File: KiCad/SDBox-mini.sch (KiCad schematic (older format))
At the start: 31 parts, among them J1 DB25_Male, J2 Conn_01x06, J3 Micro_SD_Card, J4 USB_B_Micro, Q1 BC857CW, U1 ATmega328P-AU, U2 LM1117-3.3, U3 74LVC3G17, U4 74HCT2G17, Y1 Crystal_GND24_Small

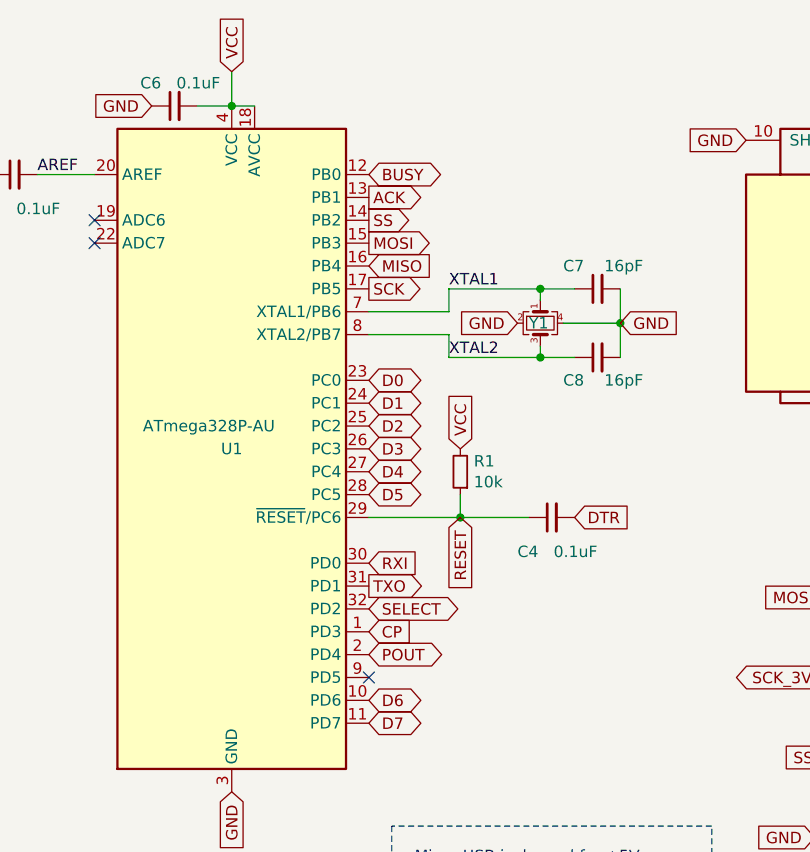
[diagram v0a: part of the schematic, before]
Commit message: Changed pin assignment BUSY from PB0 to PD4, POUT from PD4 to PD5 and rerouted due to change in FW.
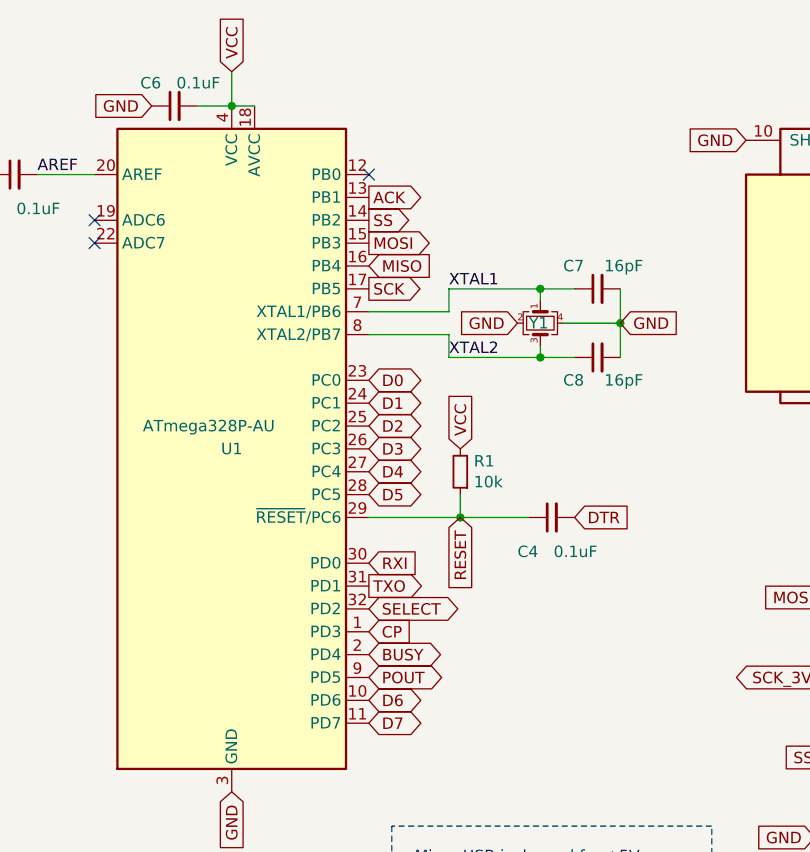
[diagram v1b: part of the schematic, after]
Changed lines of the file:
@@
 Wire Wire Line
 	5650 2250 5650 2400
+Text GLabel 4550 3800 2    50   BiDi ~ 0
+POUT
 Text GLabel 4550 3700 2    50   BiDi ~ 0
-POUT
-Text GLabel 4550 1600 2    50   BiDi ~ 0
 BUSY
 Text GLabel 4550 3300 2    50   Input ~ 0
@@
 	4950 3100 5250 3100
 Connection ~ 4950 3100
-NoConn ~ 4550 3800
+NoConn ~ 4550 1600
 NoConn ~ 7900 2350
 Text GLabel 10200 3400 2    50   Output ~ 0

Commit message: removed FTDI-header, added ICSP-header, removed hw-debounce circuit and rerouted
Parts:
- removed C11, C4: 0.1uF, Capacitor_SMD:C_0603_1608Metric_Pad1.05x0.95mm_HandSolder, symbol Device:C_Small
- removed J2: Conn_01x06, Connector_PinHeader_2.54mm:PinHeader_1x06_P2.54mm_Vertical, symbol Connector_Generic:Conn_01x06
- removed R3, R4: 10k, Resistor_SMD:R_0603_1608Metric_Pad1.05x0.95mm_HandSolder, symbol Device:R_Small
- added J2: Conn_02x03_Odd_Even, Connector_PinHeader_2.54mm:PinHeader_2x03_P2.54mm_Vertical, symbol Connector_Generic:Conn_02x03_Odd_Even
- renumbered C8 to C10, C12 to C4, C9 to C5, C10 to C6, C5 to C7, C6 to C8, C7 to C9, R5 to R3, R6 to R4, R7 to R5
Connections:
- net labels removed: CD, DTR, RXI, TXO
- wire segments 58 -> 52
- no-connect marks 14 -> 17
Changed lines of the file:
@@
 $EndDescr
 $Comp
-L Device:C_Small C5
+L Device:C_Small C7
 U 1 1 606A3110
 P 3000 1600
-F 0 "C5" V 2850 1750 50  0000 R CNN
+F 0 "C7" V 2850 1750 50  0000 R CNN
 F 1 "0.1uF" V 2850 1400 50  0000 L CNN
 F 2 "Capacitor_SMD:C_0603_1608Metric_Pad1.05x0.95mm_HandSolder" H 3000 1600 50  0001 C CNN
@@
 GND
 $Comp
-L Device:C_Small C7
+L Device:C_Small C9
 U 1 1 60FA06FB
 P 5550 2100
-F 0 "C7" V 5650 2250 50  0000 R CNN
+F 0 "C9" V 5650 2250 50  0000 R CNN
 F 1 "16pF" V 5650 1900 50  0000 L CNN
 F 2 "Capacitor_SMD:C_0603_1608Metric_Pad1.05x0.95mm_HandSolder" H 5550 2100 50  0001 C CNN
@@
 	4900 2100 5300 2100
 $Comp
-L Device:C_Small C8
+L Device:C_Small C10
 U 1 1 60FA5116
 P 5550 2400
-F 0 "C8" V 5450 2550 50  0000 R CNN
+F 0 "C10" V 5450 2550 50  0000 R CNN
 F 1 "16pF" V 5450 2200 50  0000 L CNN
 F 2 "Capacitor_SMD:C_0603_1608Metric_Pad1.05x0.95mm_HandSolder" H 5550 2400 50  0001 C CNN
@@
 Connection ~ 5650 2250
 $Comp
-L Device:C_Small C6
+L Device:C_Small C8
 U 1 1 60FA7C64
 P 3700 1300
-F 0 "C6" V 3800 1450 50  0000 R CNN
+F 0 "C8" V 3800 1450 50  0000 R CNN
 F 1 "0.1uF" V 3800 1100 50  0000 L CNN
 F 2 "Capacitor_SMD:C_0603_1608Metric_Pad1.05x0.95mm_HandSolder" H 3700 1300 50  0001 C CNN
@@
 Text GLabel 4550 3700 2    50   BiDi ~ 0
 BUSY
-Text GLabel 4550 3300 2    50   Input ~ 0
-RXI
-Text GLabel 4550 3400 2    50   Output ~ 0
-TXO
 NoConn ~ 2000 3950
 Text GLabel 4550 2000 2    50   Input ~ 0
@@
 Wire Wire Line
 	4550 2300 4900 2300
-Text GLabel 5450 3100 2    50   Input ~ 0
-DTR
-$Comp
-L Device:C_Small C4
-U 1 1 60F8E9CC
-P 5350 3100
-F 0 "C4" V 5200 3250 50  0000 R CNN
-F 1 "0.1uF" V 5200 2900 50  0000 L CNN
-F 2 "Capacitor_SMD:C_0603_1608Metric_Pad1.05x0.95mm_HandSolder" H 5350 3100 50  0001 C CNN
-F 3 "~" H 5350 3100 50  0001 C CNN
-	1    5350 3100
-	0    -1   -1   0
-$EndComp
-Text GLabel 4950 3100 3    50   Input ~ 0
+Text GLabel 4950 3100 2    50   Input ~ 0
 RESET
-Wire Wire Line
-	4950 3100 5250 3100
-Connection ~ 4950 3100
 NoConn ~ 4550 1600
 NoConn ~ 7900 2350
@@
 Text GLabel 10500 1750 2    50   Output ~ 0
 3V3
-$Comp
-L Connector_Generic:Conn_01x06 J2
-U 1 1 6104A5C2
-P 2200 5000
-F 0 "J2" H 2118 4475 50  0000 C CNN
-F 1 "Conn_01x06" H 2118 4566 50  0000 C CNN
-F 2 "Connector_PinHeader_2.54mm:PinHeader_1x06_P2.54mm_Vertical" H 2200 5000 50  0001 C CNN
-F 3 "~" H 2200 5000 50  0001 C CNN
-	1    2200 5000
-	-1   0    0    1
-$EndComp
-Text GLabel 2400 5200 2    50   Input ~ 0
-DTR
-Text GLabel 2400 5100 2    50   Input ~ 0
-TXO
-Text GLabel 2400 5000 2    50   Output ~ 0
-RXI
-Text GLabel 2400 4900 2    50   Input ~ 0
-VCC
-Text GLabel 2400 4800 2    50   Input ~ 0
-GND
-Text GLabel 2400 4700 2    50   Input ~ 0
-GND
-$Comp
-L Device:C_Small C9
+Text GLabel 3400 4950 2    50   Input ~ 0
+VCC
+Text GLabel 3400 5150 2    50   Input ~ 0
+GND
+$Comp
+L Device:C_Small C5
 U 1 1 61017825
 P 7550 3350
-F 0 "C9" H 7400 3250 50  0000 R CNN
+F 0 "C5" H 7400 3250 50  0000 R CNN
 F 1 "0.1uF" H 7200 3350 50  0000 L CNN
 F 2 "Capacitor_SMD:C_0603_1608Metric_Pad1.05x0.95mm_HandSolder" H 7550 3350 50  0001 C CNN
@@
 $EndComp
 $Comp
-L Device:C_Small C10
+L Device:C_Small C6
 U 1 1 61087309
 P 10700 3500
-F 0 "C10" H 10550 3400 50  0000 R CNN
+F 0 "C6" H 10550 3400 50  0000 R CNN
 F 1 "0.1uF" H 10350 3500 50  0000 L CNN
 F 2 "Capacitor_SMD:C_0603_1608Metric_Pad1.05x0.95mm_HandSolder" H 10700 3500 50  0001 C CNN
@@
 	9050 3400 9300 3400
 Connection ~ 9050 3400
-Text GLabel 9050 3600 0    50   Input ~ 0
-GND
-$Comp
-L Device:R_Small R4
-U 1 1 61098AA5
-P 8350 3700
-F 0 "R4" H 8291 3654 50  0000 R CNN
-F 1 "10k" H 8291 3745 50  0000 R CNN
-F 2 "Resistor_SMD:R_0603_1608Metric_Pad1.05x0.95mm_HandSolder" H 8350 3700 50  0001 C CNN
-F 3 "~" H 8350 3700 50  0001 C CNN
-	1    8350 3700
-	-1   0    0    1
-$EndComp
+Text GLabel 9300 3600 0    50   Input ~ 0
+GND
 Wire Wire Line
 	9250 1950 9250 2050
@@
 GND
 Text GLabel 7900 1450 2    50   Output ~ 0
-CD
-Text GLabel 8350 3600 1    50   Input ~ 0
-VCC
-$Comp
-L Device:R_Small R3
-U 1 1 610BDC67
-P 8800 3800
-F 0 "R3" V 8900 3850 50  0000 R CNN
-F 1 "10k" V 8700 3850 50  0000 R CNN
-F 2 "Resistor_SMD:R_0603_1608Metric_Pad1.05x0.95mm_HandSolder" H 8800 3800 50  0001 C CNN
-F 3 "~" H 8800 3800 50  0001 C CNN
-	1    8800 3800
-	0    -1   -1   0
-$EndComp
-$Comp
-L Device:C_Small C11
-U 1 1 610C0199
-P 9200 3700
-F 0 "C11" H 9400 3700 50  0000 R CNN
-F 1 "0.1uF" H 9100 3900 50  0000 L CNN
-F 2 "Capacitor_SMD:C_0603_1608Metric_Pad1.05x0.95mm_HandSolder" H 9200 3700 50  0001 C CNN
-F 3 "~" H 9200 3700 50  0001 C CNN
-	1    9200 3700
-	-1   0    0    1
-$EndComp
-Text GLabel 8200 3800 0    50   Input ~ 0
-CD
-Wire Wire Line
-	9200 3600 9300 3600
-Text GLabel 10200 3800 2    50   Output ~ 0
 CP
 Text GLabel 4550 3600 2    50   Input ~ 0
@@
 $EndComp
 $Comp
-L Device:R_Small R5
+L Device:R_Small R3
 U 1 1 60F8AA52
 P 9950 5150
-F 0 "R5" H 9891 5104 50  0000 R CNN
+F 0 "R3" H 9891 5104 50  0000 R CNN
 F 1 "150" H 9891 5195 50  0000 R CNN
 F 2 "Resistor_SMD:R_0603_1608Metric_Pad1.05x0.95mm_HandSolder" H 9950 5150 50  0001 C CNN
@@
 SS
 $Comp
-L Device:R_Small R7
+L Device:R_Small R5
 U 1 1 60FA3418
 P 8950 4850
-F 0 "R7" V 9050 4900 50  0000 R CNN
+F 0 "R5" V 9050 4900 50  0000 R CNN
 F 1 "10k" V 8850 4900 50  0000 R CNN
 F 2 "Resistor_SMD:R_0603_1608Metric_Pad1.05x0.95mm_HandSolder" H 8950 4850 50  0001 C CNN
@@
 GND
 $Comp
-L Device:R_Small R6
+L Device:R_Small R4
 U 1 1 60FB8FAC
 P 8550 5150
-F 0 "R6" H 8491 5104 50  0000 R CNN
+F 0 "R4" H 8491 5104 50  0000 R CNN
 F 1 "150" H 8491 5195 50  0000 R CNN
 F 2 "Resistor_SMD:R_0603_1608Metric_Pad1.05x0.95mm_HandSolder" H 8550 5150 50  0001 C CNN
@@
 Text Notes 9550 4350 0    50   ~ 0
 Optional Power LED indicator
-Wire Wire Line
-	8200 3800 8350 3800
-Wire Wire Line
-	8350 3800 8700 3800
-Connection ~ 8350 3800
-Wire Wire Line
-	8900 3800 9200 3800
-Connection ~ 9200 3800
-Wire Wire Line
-	9200 3800 9300 3800
-Wire Wire Line
-	9050 3600 9200 3600
-Connection ~ 9200 3600
 Text Notes 4750 4700 0    50   ~ 0
 Micro-USB jack used for +5V \npower supply only. Mandatory
@@
 	6050 6000 6050 4450
 $Comp
-L SDBox-mini:T491D227K010AT C12
+L SDBox-mini:T491D227K010AT C4
 U 1 1 60F9E387
 P 6300 5300
-F 0 "C12" V 6450 5050 50  0000 C CNN
+F 0 "C4" V 6450 5050 50  0000 C CNN
 F 1 "T491D227K010AT" V 6350 4800 50  0000 C CNN
 F 2 "SDBox-mini:CAPMP7343X430N" H 6300 5300 50  0001 L BNN
@@
 	6300 5700 6300 5400
 Connection ~ 5050 5700
+$Comp
+L Connector_Generic:Conn_02x03_Odd_Even J2
+U 1 1 610260A5
+P 3100 5050
+F 0 "J2" H 3150 5367 50  0000 C CNN
+F 1 "Conn_02x03_Odd_Even" H 3150 5276 50  0000 C CNN
+F 2 "Connector_PinHeader_2.54mm:PinHeader_2x03_P2.54mm_Vertical" H 3100 5050 50  0001 C CNN
+F 3 "~" H 3100 5050 50  0001 C CNN
+	1    3100 5050
+	1    0    0    -1
+$EndComp
+Text GLabel 2900 5150 0    50   Input ~ 0
+RESET
+Text GLabel 2900 5050 0    50   Input ~ 0
+SCK
+Text GLabel 2900 4950 0    50   Output ~ 0
+MISO
+Text GLabel 3400 5050 2    50   Input ~ 0
+MOSI
+Wire Wire Line
+	9300 3800 9300 3600
+NoConn ~ 10200 3800
+NoConn ~ 4550 3300
+NoConn ~ 4550 3400
 $EndSCHEMATC

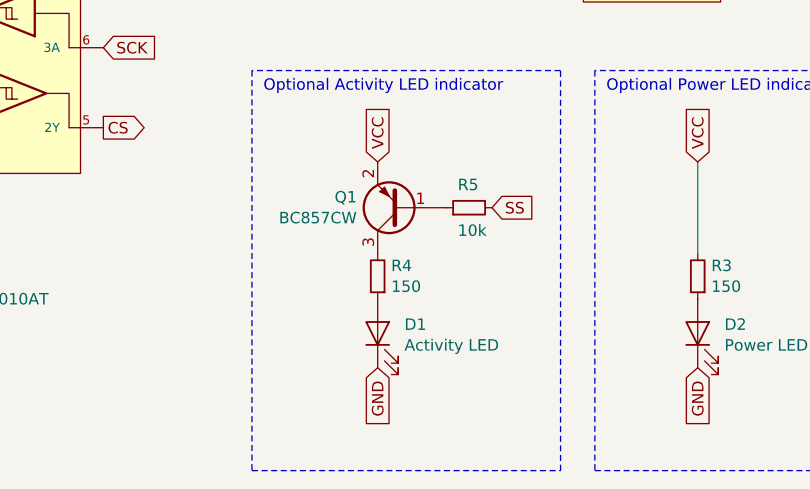
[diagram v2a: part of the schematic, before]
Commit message: removed transistor Q1, changed Activity LED circuit to sink by SS
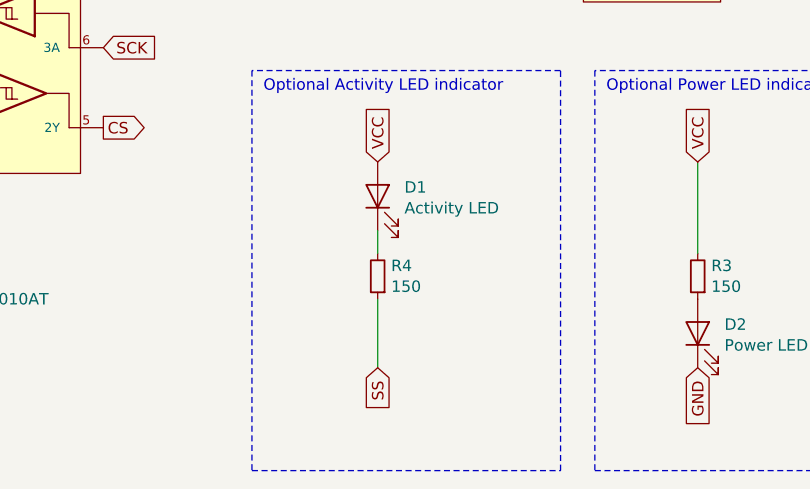
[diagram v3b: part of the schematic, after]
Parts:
- removed Q1: BC857CW, Package_TO_SOT_SMD:SOT-323_SC-70_Handsoldering, symbol Transistor_BJT:BC857W
- removed R5: 10k, Resistor_SMD:R_0603_1608Metric_Pad1.05x0.95mm_HandSolder, symbol Device:R_Small
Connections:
- net +5V: now also D1.2 (A)
- net GND: no longer D1.1 (K)
- net SS: now also R4.1
- net at R4.2: now also D1.1 (K)
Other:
- moved on the sheet: D1
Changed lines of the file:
@@
 Text GLabel 8550 4650 1    50   Input ~ 0
 VCC
-Text GLabel 9050 4850 2    50   Input ~ 0
+Text GLabel 8550 5550 3    50   Input ~ 0
 SS
-$Comp
-L Device:R_Small R5
-U 1 1 60FA3418
-P 8950 4850
-F 0 "R5" V 9050 4900 50  0000 R CNN
-F 1 "10k" V 8850 4900 50  0000 R CNN
-F 2 "Resistor_SMD:R_0603_1608Metric_Pad1.05x0.95mm_HandSolder" H 8950 4850 50  0001 C CNN
-F 3 "~" H 8950 4850 50  0001 C CNN
-	1    8950 4850
-	0    -1   -1   0
-$EndComp
-$Comp
-L Transistor_BJT:BC857W Q1
-U 1 1 60FA42A1
-P 8650 4850
-F 0 "Q1" H 8841 4804 50  0000 L CNN
-F 1 "BC857CW" H 8841 4895 50  0000 L CNN
-F 2 "Package_TO_SOT_SMD:SOT-323_SC-70_Handsoldering" H 8850 4775 50  0001 L CIN
-F 3 "http://www.infineon.com/dgdl/Infineon-BC857SERIES_BC858SERIES_BC859SERIES_BC860SERIES-DS-v01_01-en.pdf?fileId=db3a304314dca389011541da0e3a1661" H 8650 4850 50  0001 L CNN
-	1    8650 4850
-	-1   0    0    1
-$EndComp
 $Comp
 L Device:LED D1
 U 1 1 60FB07A5
-P 8550 5400
-F 0 "D1" V 8589 5283 50  0000 R CNN
-F 1 "Activity LED" V 8498 5283 50  0000 R CNN
-F 2 "Connector_PinHeader_2.54mm:PinHeader_1x02_P2.54mm_Vertical" H 8550 5400 50  0001 C CNN
-F 3 "~" H 8550 5400 50  0001 C CNN
-	1    8550 5400
+P 8550 4800
+F 0 "D1" V 8589 4683 50  0000 R CNN
+F 1 "Activity LED" V 8498 4683 50  0000 R CNN
+F 2 "Connector_PinHeader_2.54mm:PinHeader_1x02_P2.54mm_Vertical" H 8550 4800 50  0001 C CNN
+F 3 "~" H 8550 4800 50  0001 C CNN
+	1    8550 4800
 	0    -1   -1   0
 $EndComp
-Text GLabel 8550 5550 3    50   Input ~ 0
-GND
 $Comp
 L Device:R_Small R4
@@
 NoConn ~ 4550 3300
 NoConn ~ 4550 3400
+Wire Wire Line
+	8550 4950 8550 5050
+Wire Wire Line
+	8550 5250 8550 5550
 $EndSCHEMATC
